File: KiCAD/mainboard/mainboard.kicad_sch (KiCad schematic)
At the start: 0 parts

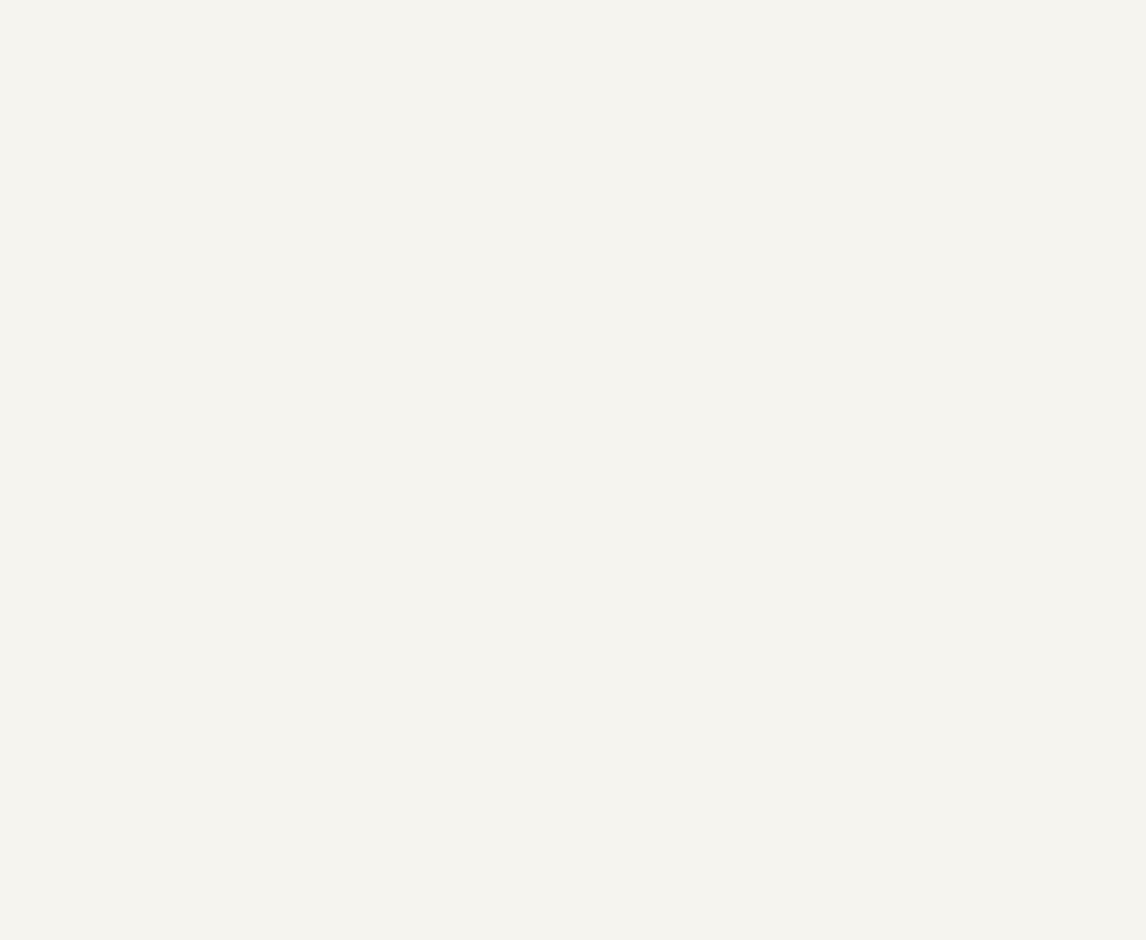
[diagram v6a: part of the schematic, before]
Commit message: Changed all FPGA Connections to what we want, created a new project for the connection board
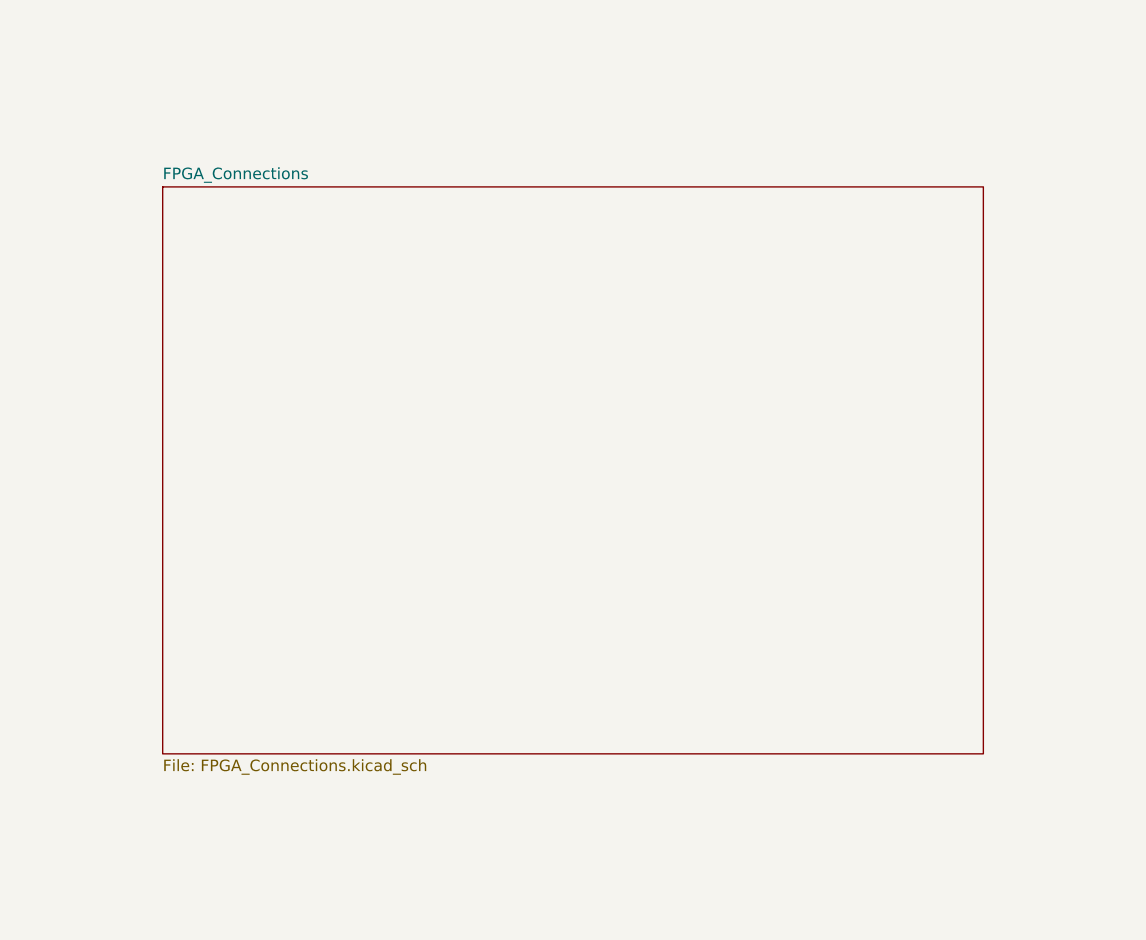
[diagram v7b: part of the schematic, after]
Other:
- added sheet FPGA_Connections (FPGA_Connections.kicad_sch)
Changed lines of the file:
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@@
+	)
+	(sheet
+		(at 198.12 169.164)
+		(size 91.186 62.992)
+		(exclude_from_sim no)
+		(in_bom yes)
+		(on_board yes)
+		(dnp no)
+		(fields_autoplaced yes)
+		(stroke
+			(width 0.1524)
+			(type solid)
+		)
+		(fill
+			(color 0 0 0 0.0000)
+		)
+		(property "Sheetname" "FPGA_Connections"
+			(at 198.12 168.4524 0)
+			(effects
+				(font
+					(size 1.27 1.27)
+				)
+				(justify left bottom)
+			)
+		)
+		(property "Sheetfile" "FPGA_Connections.kicad_sch"
+			(at 198.12 232.7406 0)
+			(effects
+				(font
+					(size 1.27 1.27)
+				)
+				(justify left top)
+			)
+		)
+		(instances
+			(project "mainboard"
+				(path "/38e83f42-2cf9-4799-a46f-ca415d95b90a"
+					(page "6")
+				)
+			)
+		)
 	)
 	(sheet

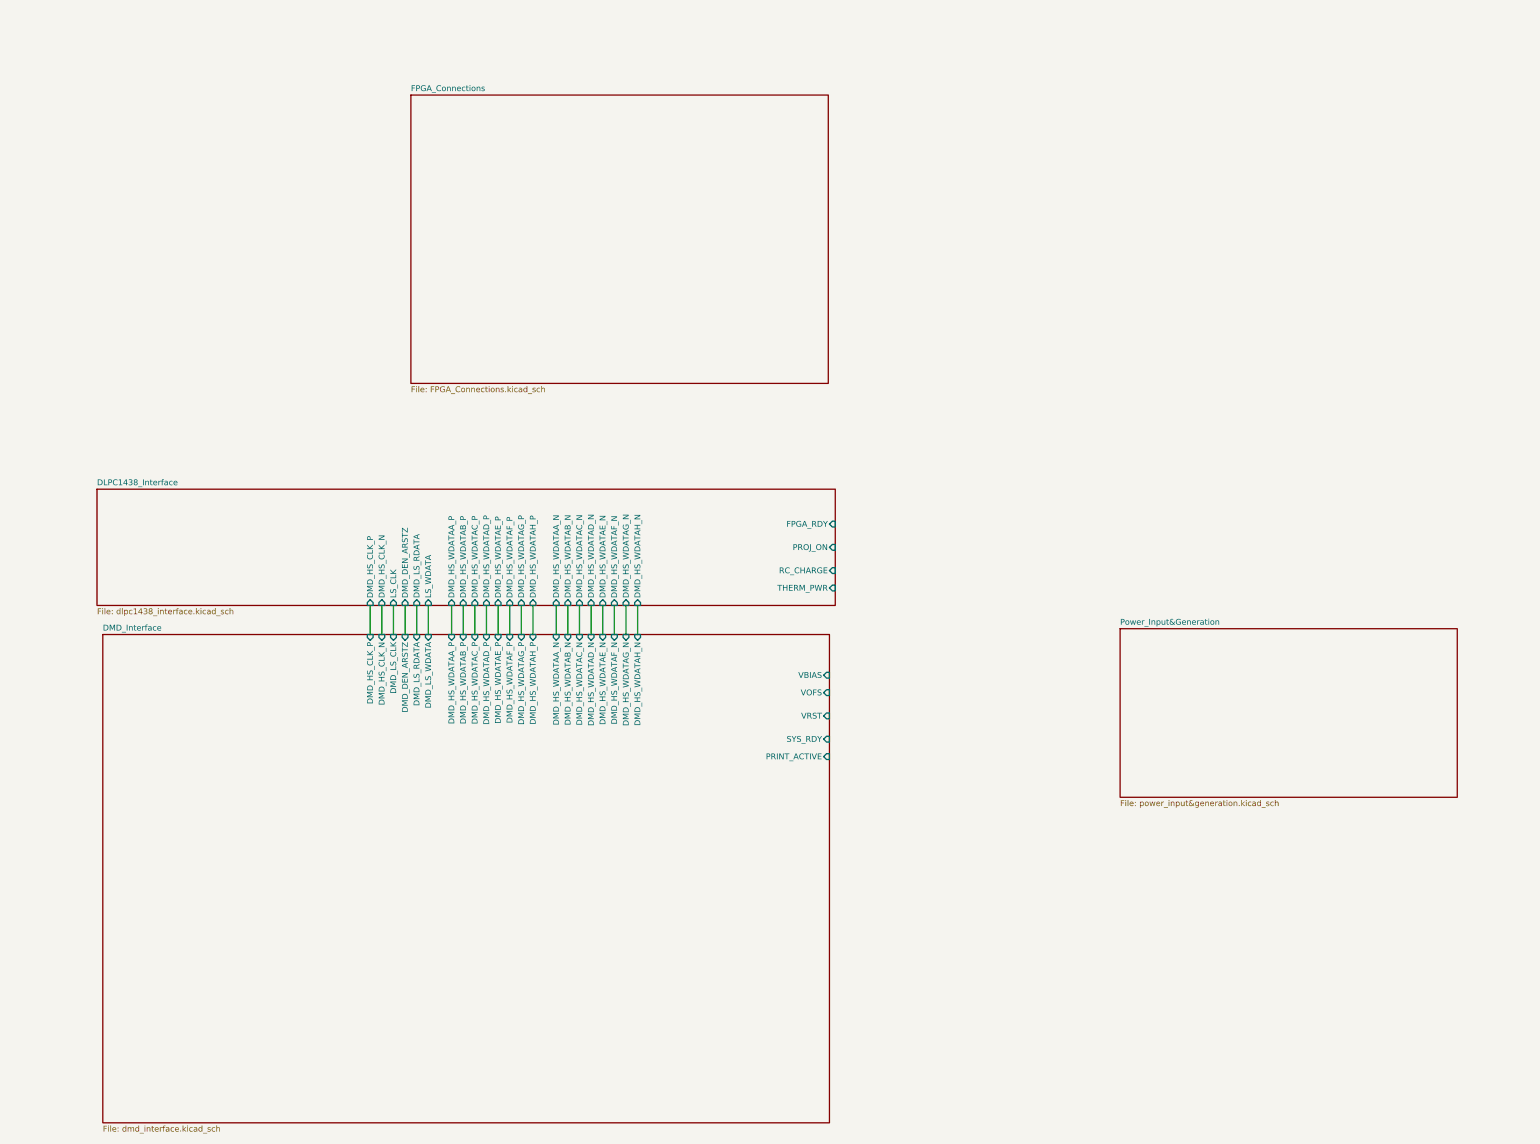
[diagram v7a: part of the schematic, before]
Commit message: fixed pdata bus connection
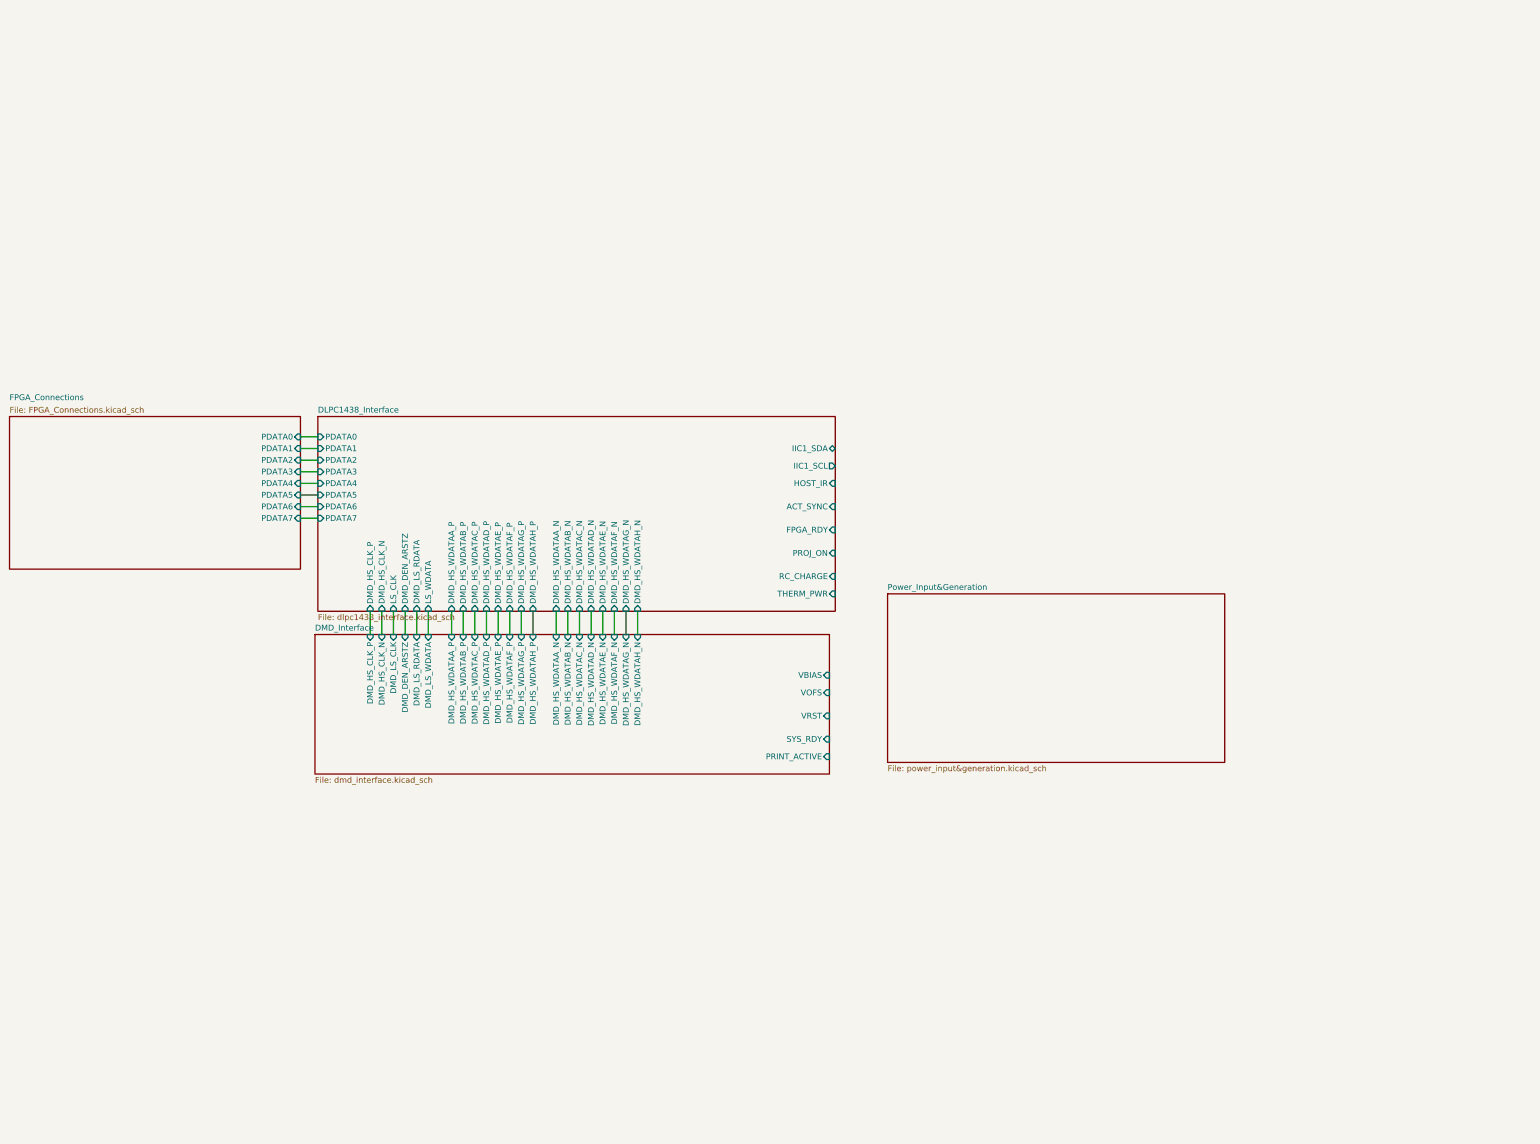
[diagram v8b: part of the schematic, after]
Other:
- sheet DLPC1438_Interface ports: added ACT_SYNC, HOST_IR, IIC1_SCL, IIC1_SDA, PDATA0, PDATA1, PDATA2, PDATA3, PDATA4, PDATA5, PDATA6, PDATA7; removed none
- sheet FPGA_Connections ports: added PDATA0, PDATA1, PDATA2, PDATA3, PDATA4, PDATA5, PDATA6, PDATA7; removed none
